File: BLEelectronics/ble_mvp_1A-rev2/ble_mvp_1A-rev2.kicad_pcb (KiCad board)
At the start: 2 copper layers, 45.3 x 27.5 mm, 19 parts, among them IC1 LTC4412xS6, IC2 PCF8523T, IC3 MX25R6435FM2IL0, J1 Nordic_nRF52840_breakout, Q1 Si2307CDS, U1 LP5907MFX-3.3, U2 BAT-HLD-001, U3 ESD401, U4 ESD401, X1 32.768KHZ

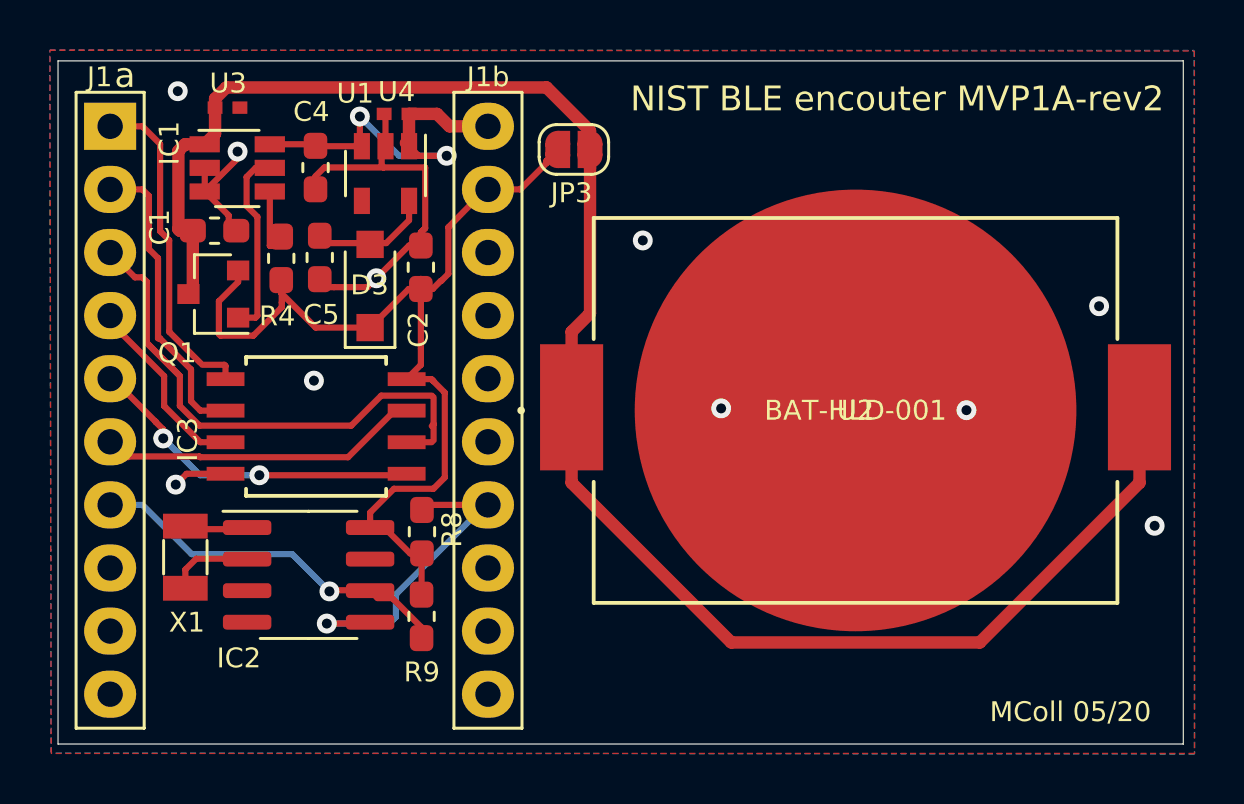
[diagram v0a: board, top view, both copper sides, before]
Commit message: MVP1A-rev2 ready for fab/assembly. DRC clean, .pos clean, BOM clean.
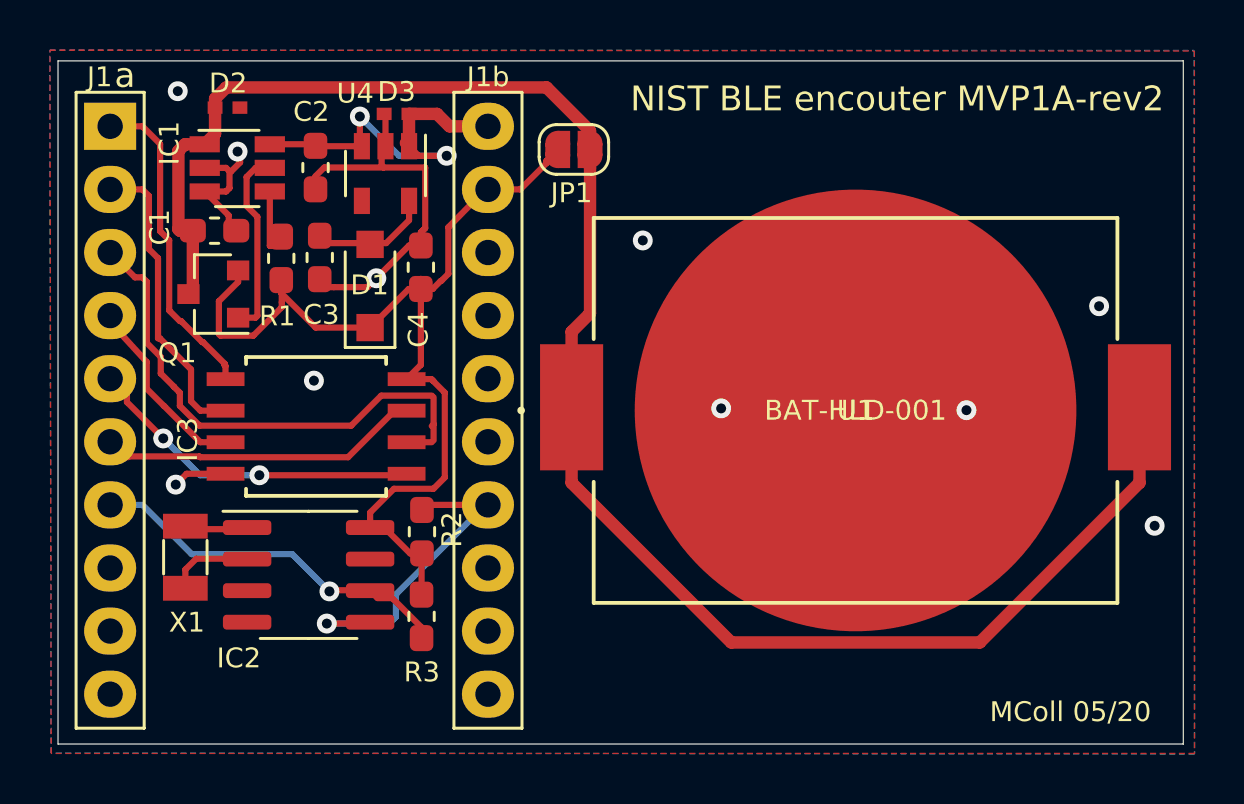
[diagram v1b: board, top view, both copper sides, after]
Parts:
- renumbered C4 to C2, C5 to C3, C2 to C4, D3 to D1, U3 to D2, U4 to D3, JP3 to JP1, R4 to R1, R8 to R2, R9 to R3, U2 to U1, U1 to U4
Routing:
- net /SCLK: track 23.1 -> 21.3 mm
- net GND: track 23.2 -> 24.2 mm
